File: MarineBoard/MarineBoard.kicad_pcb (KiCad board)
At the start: 4 copper layers, 66.5 x 70 mm, 148 parts, among them CN1 MKDSN 1,5/ 2-5,08, CN2 MKDSN 1,5/ 2-5,08, CN3 SM04B-SRSS-TB (LF)(SN), J1 USB_C_Receptacle_USB2.0_16P, J3 Conn_02x09_Top_Bottom, Q1 IPL60R075CFD7, Q2 S8050, Q3 S8050, U1 SY8089A1AAC, U10 PC817C-S, U11 SN65HVD230DR, U12 DB125-3.5-3P-GN-S, U13 DB125-3.5-3P-GN-S, U14 PC817C-S, U15 TC4427EPA, U16 PC817C-S, U17 PC817C-S, U18 INA226, U19 INA226, U2 INA226, U3 TPS5430DDA, U4 DB125-3.5-2P-GN-S, U5 DB125-3.5-2P-GN-S, U6 DB125-3.5-2P-GN-S, U7 DB125-3.5-3P-GN-S, U8 ESP32-S3-WROOM-2-N32R16V, U9 DB125-3.5-3P-GN-S

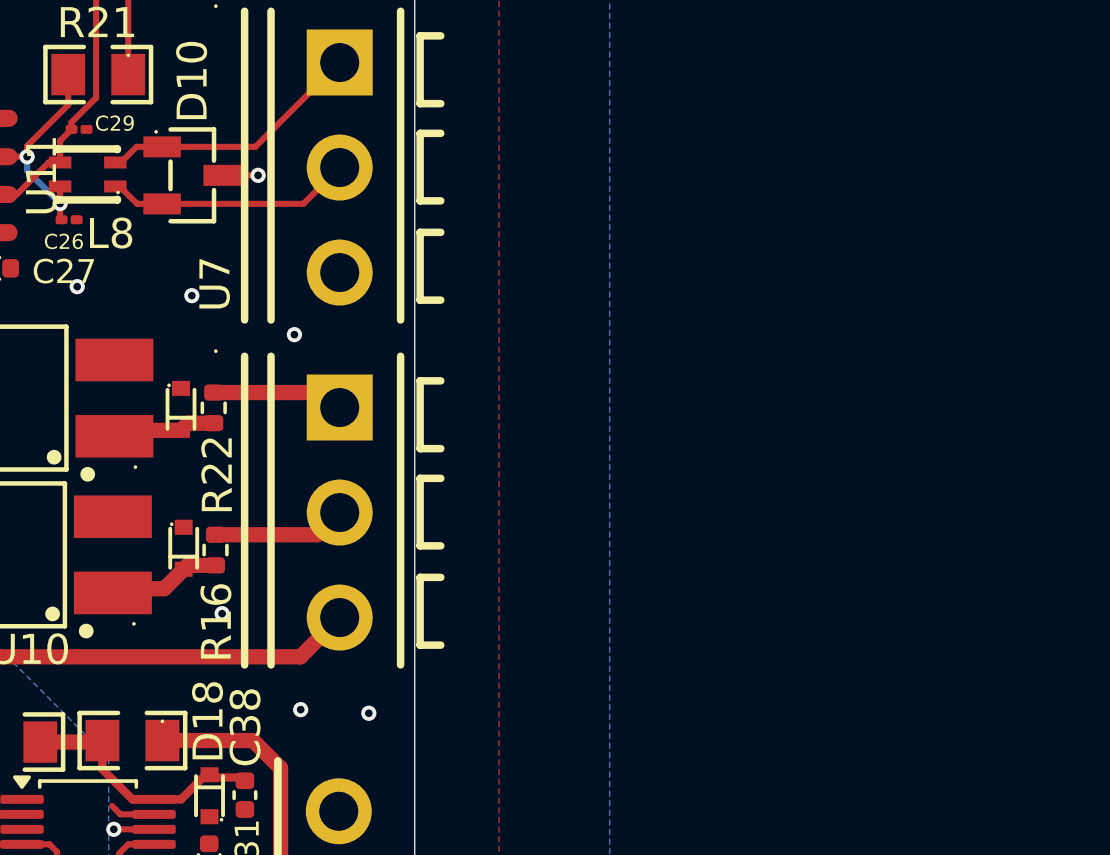
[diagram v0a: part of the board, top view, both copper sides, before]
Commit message: MarineBoard: update KiCad project + add EasyEDA library assets
- Update PCB, schematic, project, and library-table files
- Add EasyEDA symbol/footprint/3D-model assets (C0402, C1210, R2512, SMA)
- Add new documentation images (ESP32, FSPI, RPM)

Co-Authored-By: Claude Sonnet 5 <noreply@anthropic.com>
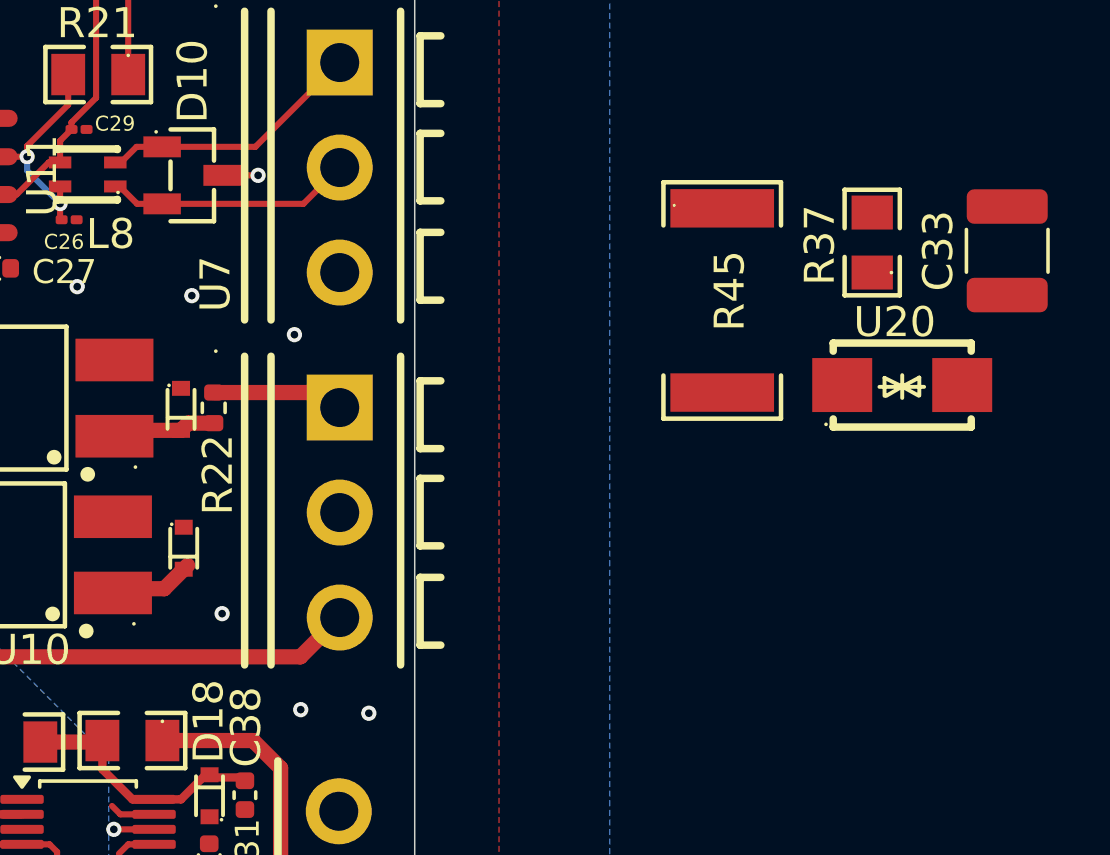
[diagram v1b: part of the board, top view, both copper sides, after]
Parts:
- removed R16: 1K, Resistor_SMD:R_0402_1005Metric
- added C33: 1.2uF 100V, Capacitor_SMD:C_1210_3225Metric, F.Cu at (186.8, 53.8)
- added R37: 100K, easyeda2kicad:R0805, F.Cu at (182.2, 53.5)
- added R45: 2K2, EasyEDA:R2512, F.Cu at (177.2, 55.4)
- added U20: SMAJ6.8CA, EasyEDA:SMA_L4.4-W2.6-LS5.0-BI, F.Cu at (183.2, 58.2)
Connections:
- U13 pad 2: RPM -> SH+
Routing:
- net RPM: track 4.45 -> 0.00 mm
- net Net-(D8-K): track 3.80 -> 2.87 mm
